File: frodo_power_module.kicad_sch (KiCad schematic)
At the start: 61 parts, among them J1 Keystone 1098, J10 SWD Header, J2 Molex MicroFit 2x2, J3 Molex MicroFit 2x2, J4 Molex MicroFit 2x2, J5 Molex MicroFit 2x2, J6 Molex MicroFit 2x2, J7 JST-GH, J8 JST-GH, J9 JST-GH, U1 STM32F042F6Px, U2 L7805, U3 AZ1117I-3.3, U4 BQ25171-Q1, U5 BQ29200, U6 MCP2562-E-SN, Y1 8MHz

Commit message: Add current sense amp to PCB
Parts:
- added C18, C19, C20: 100n, Capacitor_SMD:C_0603_1608Metric, symbol Device:C_Small
- added R18, R19: 10k, Resistor_SMD:R_0603_1608Metric, symbol Device:R_Small
- added R20, R22, R24: 1k8, Resistor_SMD:R_0603_1608Metric, symbol Device:R_Small
- added R21, R23: 1k, Resistor_SMD:R_0603_1608Metric, symbol Device:R_Small
- added U7: INA213, Package_TO_SOT_SMD:SOT-363_SC-70-6, symbol frodo_power_module:INA210
- R10, R14, R17: LCSC# C98220 -> (none); Part# RC0603FR-0710KL -> (none)
- R13: value TODO -> 5m
- R15: value 160 -> 120; LCSC# C98220 -> C114640; Part# RC0603FR-0710KL -> RC0603FR-07120RL
- R16: value 260 -> 220
- R2: LCSC# C114640 -> C98220; Part# RC0603FR-07120RL -> RC0603FR-0710KL
- R6: value 3.6k -> 1k8; LCSC# C98220 -> C185354; Part# RC0603FR-0710KL -> RC0603FR-071K8L
- R7, R8: value 1k -> 220
- R9: LCSC# C98220 -> (none); Manufacturer YAGEO -> (none); Part# RC0603FR-0710KL -> (none)
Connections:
- net +3V3: now also C18.2, C20.2, R18.2, U7.3 (V+)
- net +5V: now also C19.2
- net +BATT: now also U7.5 (-)
- net +VSW: now also R22.1
- net GND: now also C18.1, C19.1, C20.1, R19.1, R21.2, R23.2, R24.2, U7.2 (GND); no longer R6.2, R7.2
- net VDC: now also C12.1, D1.1 (K), JP1.1 (A), U4.1 (IN), R20.1; no longer D1.2 (A), J2.3 (Pin_3), J2.4 (Pin_4)
- net at R7.1, U4.2 (ISET): no longer R8.1
- net VSENSE_CHARGE: now reaches U1.12 (PA6)
- net VSENSE_CHARGE: now also R20.2, R21.1
- net VSENSE_BATT: now reaches U1.13 (PA7)
- net VSENSE_BATT: now also R22.2, R23.1
- net ISENSE: now reaches U1.14 (PB1)
- net ISENSE: now also U7.6
- net BATT_RAW: no longer names the net of J1.1 (Pin_1), R13.2, R14.2, R15.2
- net BATT_RAW: now also U7.4 (+)
- new net: R18.1, R19.2, U7.1 (REF)
- new net: R24.1, R6.2
- new net: R7.2, R8.1
- new net: D1.2 (A), J2.3 (Pin_3), J2.4 (Pin_4)
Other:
- note added: "ISET: 440 = 681mA"
- note added: "Icb1 = Vc1 / (Rcb + Rc1) Icb2 = (Vc2-Vc1) / (Rcb + Rvdd + Rc2) Icb1 = Icb2 => Rc1 = Rvdd + Rc2"
- note added: "max shunt drop: 3.3V (ADC range) / 2 (bidirectional) / 50 (INA gain) = 33mV max current: 33mV / 5mOhm = +/-6.6A, resolution: 6.6A/2048 = ~3.2mA"
- note removed: "ISET: 500 = 600mA"
- note removed: "TODO: Use current sense amplifier? INA210?"
- note removed: "TODO: pins for battery and charging voltage, current"
- moved on the sheet: C12, D1, R7, R8

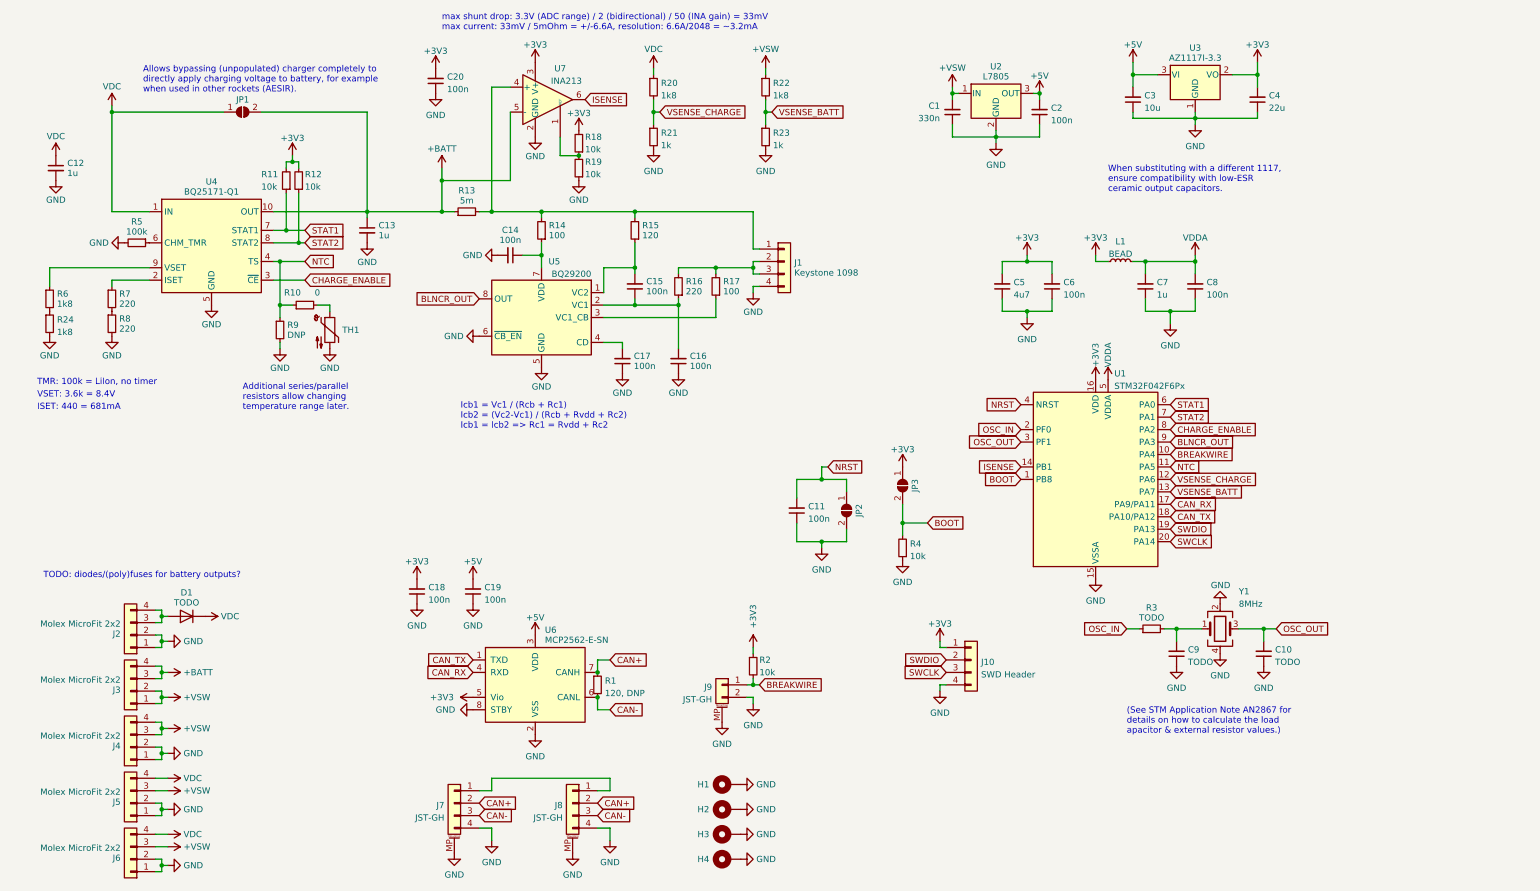
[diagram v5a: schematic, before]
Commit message: changed PCB
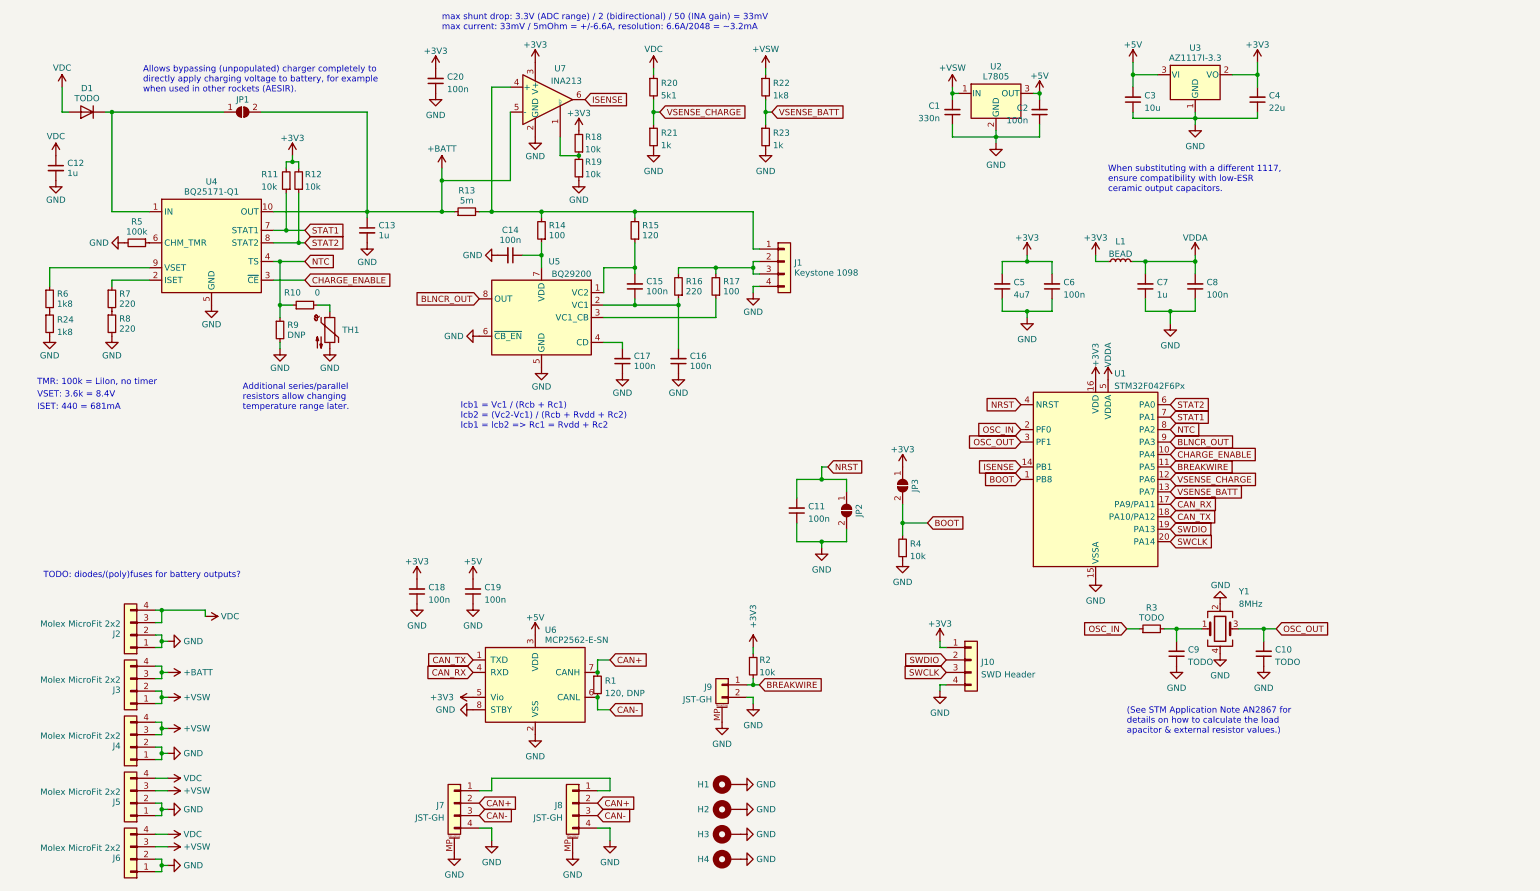
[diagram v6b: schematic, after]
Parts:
- R20: value 1k8 -> 5k1
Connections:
- net BREAKWIRE: now also U1.11 (PA5); no longer U1.10 (PA4)
- net CHARGE_ENABLE: now also U1.10 (PA4); no longer U1.8 (PA2)
- net NTC: now also U1.8 (PA2); no longer U1.11 (PA5)
- net STAT1: now also U1.7 (PA1); no longer U1.6 (PA0)
- net STAT2: now also U1.6 (PA0); no longer U1.7 (PA1)
- net VDC: now also D1.2 (A), J2.3 (Pin_3), J2.4 (Pin_4); no longer D1.1 (K), JP1.1 (A), U4.1 (IN)
- new net: D1.1 (K), JP1.1 (A), U4.1 (IN)
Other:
- moved on the sheet: C2, D1
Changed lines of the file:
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@@
   (junction (at 255.27 66.04) (diameter 0) (color 0 0 0 0)
   )
+  (junction (at 44.45 137.16) (diameter 0) (color 0 0 0 0)
+  )
   (junction (at 220.98 66.04) (diameter 0) (color 0 0 0 0)
   )
@@
   (junction (at 255.27 36.83) (diameter 0) (color 0 0 0 0)
   )
-  (junction (at 34.29 35.56) (diameter 0) (color 0 0 0 0)
-  )
   (junction (at 179.07 110.49) (diameter 0) (color 0 0 0 0)
   )
@@
   (junction (at 269.24 140.97) (diameter 0) (color 0 0 0 0)
   )
-  (junction (at 44.45 138.43) (diameter 0) (color 0 0 0 0)
-  )
   (junction (at 220.98 76.2) (diameter 0) (color 0 0 0 0)
   )
@@
   (junction (at 44.45 189.23) (diameter 0) (color 0 0 0 0)
   )
+  (junction (at 34.29 35.56) (diameter 0) (color 0 0 0 0)
+  )
   (junction (at 69.85 59.69) (diameter 0) (color 0 0 0 0)
   )
@@
     (stroke (width 0) (type default))
   )
-  (wire (pts (xy 44.45 137.16) (xy 44.45 138.43))
+  (wire (pts (xy 24.13 35.56) (xy 25.4 35.56))
+    (stroke (width 0) (type default))
+  )
+  (wire (pts (xy 44.45 137.16) (xy 44.45 139.7))
     (stroke (width 0) (type default))
   )
@@
     (stroke (width 0) (type default))
   )
-  (wire (pts (xy 45.72 138.43) (xy 44.45 138.43))
-    (stroke (width 0) (type default))
-  )
   (wire (pts (xy 44.45 160.02) (xy 43.18 160.02))
     (stroke (width 0) (type default))
@@
     (stroke (width 0) (type default))
   )
+  (wire (pts (xy 53.34 137.16) (xy 53.34 138.43))
+    (stroke (width 0) (type default))
+  )
   (wire (pts (xy 44.45 154.94) (xy 44.45 156.21))
     (stroke (width 0) (type default))
@@
     (stroke (width 0) (type default))
   )
-  (wire (pts (xy 44.45 138.43) (xy 44.45 139.7))
-    (stroke (width 0) (type default))
-  )
   (wire (pts (xy 220.98 76.2) (xy 220.98 77.47))
     (stroke (width 0) (type default))
@@
     (stroke (width 0) (type default))
   )
+  (wire (pts (xy 44.45 137.16) (xy 53.34 137.16))
+    (stroke (width 0) (type default))
+  )
   (wire (pts (xy 44.45 167.64) (xy 43.18 167.64))
     (stroke (width 0) (type default))
@@
     (stroke (width 0) (type default))
   )
-  (wire (pts (xy 34.29 34.29) (xy 34.29 35.56))
+  (wire (pts (xy 24.13 30.48) (xy 24.13 35.56))
     (stroke (width 0) (type default))
   )
@@
     (stroke (width 0) (type default))
   )
+  (wire (pts (xy 33.02 35.56) (xy 34.29 35.56))
+    (stroke (width 0) (type default))
+  )
   (wire (pts (xy 68.58 66.04) (xy 73.66 66.04))
     (stroke (width 0) (type default))
@@
     )
   )
-  (global_label "STAT2" (shape input) (at 250.19 97.79 0) (fields_autoplaced)
+  (global_label "STAT2" (shape input) (at 250.19 95.25 0) (fields_autoplaced)
     (effects (font (size 1.27 1.27)) (justify left))
-    (property "Intersheetrefs" "${INTERSHEET_REFS}" (at 258.5386 97.79 0)
+    (property "Intersheetrefs" "${INTERSHEET_REFS}" (at 258.5386 95.25 0)
       (effects (font (size 1.27 1.27)) (justify left) hide)
     )
@@
     )
   )
-  (global_label "STAT1" (shape input) (at 250.19 95.25 0) (fields_autoplaced)
+  (global_label "STAT1" (shape input) (at 250.19 97.79 0) (fields_autoplaced)
     (effects (font (size 1.27 1.27)) (justify left))
-    (property "Intersheetrefs" "${INTERSHEET_REFS}" (at 258.5386 95.25 0)
+    (property "Intersheetrefs" "${INTERSHEET_REFS}" (at 258.5386 97.79 0)
       (effects (font (size 1.27 1.27)) (justify left) hide)
     )
@@
     )
   )
-  (global_label "NTC" (shape input) (at 250.19 107.95 0) (fields_autoplaced)
+  (global_label "NTC" (shape input) (at 250.19 100.33 0) (fields_autoplaced)
     (effects (font (size 1.27 1.27)) (justify left))
-    (property "Intersheetrefs" "${INTERSHEET_REFS}" (at 256.6639 107.95 0)
+    (property "Intersheetrefs" "${INTERSHEET_REFS}" (at 256.6639 100.33 0)
       (effects (font (size 1.27 1.27)) (justify left) hide)
     )
@@
     )
   )
+  (global_label "BREAKWIRE" (shape input) (at 250.19 107.95 0) (fields_autoplaced)
+    (effects (font (size 1.27 1.27)) (justify left))
+    (property "Intersheetrefs" "${INTERSHEET_REFS}" (at 263.6186 107.95 0)
+      (effects (font (size 1.27 1.27)) (justify left) hide)
+    )
+  )
   (global_label "OSC_IN" (shape input) (at 219.71 100.33 180) (fields_autoplaced)
     (effects (font (size 1.27 1.27)) (justify right))
@@
     )
   )
-  (global_label "BREAKWIRE" (shape input) (at 250.19 105.41 0) (fields_autoplaced)
-    (effects (font (size 1.27 1.27)) (justify left))
-    (property "Intersheetrefs" "${INTERSHEET_REFS}" (at 263.6186 105.41 0)
-      (effects (font (size 1.27 1.27)) (justify left) hide)
-    )
-  )
   (global_label "OSC_OUT" (shape input) (at 219.71 102.87 180) (fields_autoplaced)
     (effects (font (size 1.27 1.27)) (justify right))
@@
     )
   )
+  (global_label "CHARGE_ENABLE" (shape input) (at 250.19 105.41 0) (fields_autoplaced)
+    (effects (font (size 1.27 1.27)) (justify left))
+    (property "Intersheetrefs" "${INTERSHEET_REFS}" (at 268.4567 105.41 0)
+      (effects (font (size 1.27 1.27)) (justify left) hide)
+    )
+  )
   (global_label "BLNCR_OUT" (shape input) (at 109.22 73.66 180) (fields_autoplaced)
     (effects (font (size 1.27 1.27)) (justify right))
@@
     )
   )
-  (global_label "CHARGE_ENABLE" (shape input) (at 250.19 100.33 0) (fields_autoplaced)
-    (effects (font (size 1.27 1.27)) (justify left))
-    (property "Intersheetrefs" "${INTERSHEET_REFS}" (at 268.4567 100.33 0)
-      (effects (font (size 1.27 1.27)) (justify left) hide)
-    )
-  )
   (global_label "BLNCR_OUT" (shape input) (at 250.19 102.87 0) (fields_autoplaced)
     (effects (font (size 1.27 1.27)) (justify left))
@@
     )
   )
-  (symbol (lib_id "Device:C_Small") (at 223.52 35.56 180) (unit 1)
-    (in_bom yes) (on_board yes) (dnp no) (fields_autoplaced)
-    (property "Reference" "C2" (at 225.8441 34.7189 0)
+  (symbol (lib_id "Device:C_Small") (at 223.52 35.56 0) (mirror x) (unit 1)
+    (in_bom yes) (on_board yes) (dnp no)
+    (property "Reference" "C2" (at 221.1959 34.7189 0)
       (effects (font (size 1.27 1.27)) (justify right))
     )
-    (property "Value" "100n" (at 225.8441 37.2558 0)
+    (property "Value" "100n" (at 221.1959 37.2558 0)
       (effects (font (size 1.27 1.27)) (justify right))
     )
@@
   )
   (symbol (lib_id "power:VDDA") (at 255.27 64.77 0) (unit 1)
-    (in_bom yes) (on_board yes) (dnp no) (fields_autoplaced)
+    (in_bom yes) (on_board yes) (dnp no)
     (property "Reference" "#PWR040" (at 255.27 68.58 0)
       (effects (font (size 1.27 1.27)) hide)
@@
     )
   )
-  (symbol (lib_id "Device:D") (at 49.53 138.43 180) (unit 1)
+  (symbol (lib_id "Device:D") (at 29.21 35.56 180) (unit 1)
     (in_bom yes) (on_board yes) (dnp no) (fields_autoplaced)
-    (property "Reference" "D1" (at 49.53 133.58 0)
+    (property "Reference" "D1" (at 29.21 30.71 0)
       (effects (font (size 1.27 1.27)))
     )
-    (property "Value" "TODO" (at 49.53 135.628 0)
+    (property "Value" "TODO" (at 29.21 32.758 0)
       (effects (font (size 1.27 1.27) (color 194 0 0 1)))
     )
-    (property "Footprint" "" (at 49.53 138.43 0)
+    (property "Footprint" "" (at 29.21 35.56 0)
       (effects (font (size 1.27 1.27)) hide)
     )
-    (property "Datasheet" "~" (at 49.53 138.43 0)
+    (property "Datasheet" "~" (at 29.21 35.56 0)
       (effects (font (size 1.27 1.27)) hide)
     )
-    (property "Sim.Device" "D" (at 49.53 138.43 0)
+    (property "Sim.Device" "D" (at 29.21 35.56 0)
       (effects (font (size 1.27 1.27)) hide)
     )
-    (property "Sim.Pins" "1=K 2=A" (at 49.53 138.43 0)
+    (property "Sim.Pins" "1=K 2=A" (at 29.21 35.56 0)
       (effects (font (size 1.27 1.27)) hide)
     )
@@
     )
   )
-  (symbol (lib_id "power:VDC") (at 34.29 34.29 0) (unit 1)
+  (symbol (lib_id "power:VDC") (at 24.13 30.48 0) (unit 1)
     (in_bom yes) (on_board yes) (dnp no) (fields_autoplaced)
-    (property "Reference" "#PWR011" (at 34.29 36.83 0)
+    (property "Reference" "#PWR011" (at 24.13 33.02 0)
       (effects (font (size 1.27 1.27)) hide)
     )
-    (property "Value" "VDC" (at 34.29 30.345 0)
+    (property "Value" "VDC" (at 24.13 26.535 0)
       (effects (font (size 1.27 1.27)))
     )
-    (property "Footprint" "" (at 34.29 34.29 0)
+    (property "Footprint" "" (at 24.13 30.48 0)
       (effects (font (size 1.27 1.27)) hide)
     )
-    (property "Datasheet" "" (at 34.29 34.29 0)
+    (property "Datasheet" "" (at 24.13 30.48 0)
       (effects (font (size 1.27 1.27)) hide)
     )
@@
       (effects (font (size 1.27 1.27)) (justify left))
     )
-    (property "Value" "1k8" (at 146.2786 32.1822 0)
+    (property "Value" "5k1" (at 146.2786 32.1822 0)
       (effects (font (size 1.27 1.27)) (justify left))
     )

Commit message: Update PCB design, add LEDs
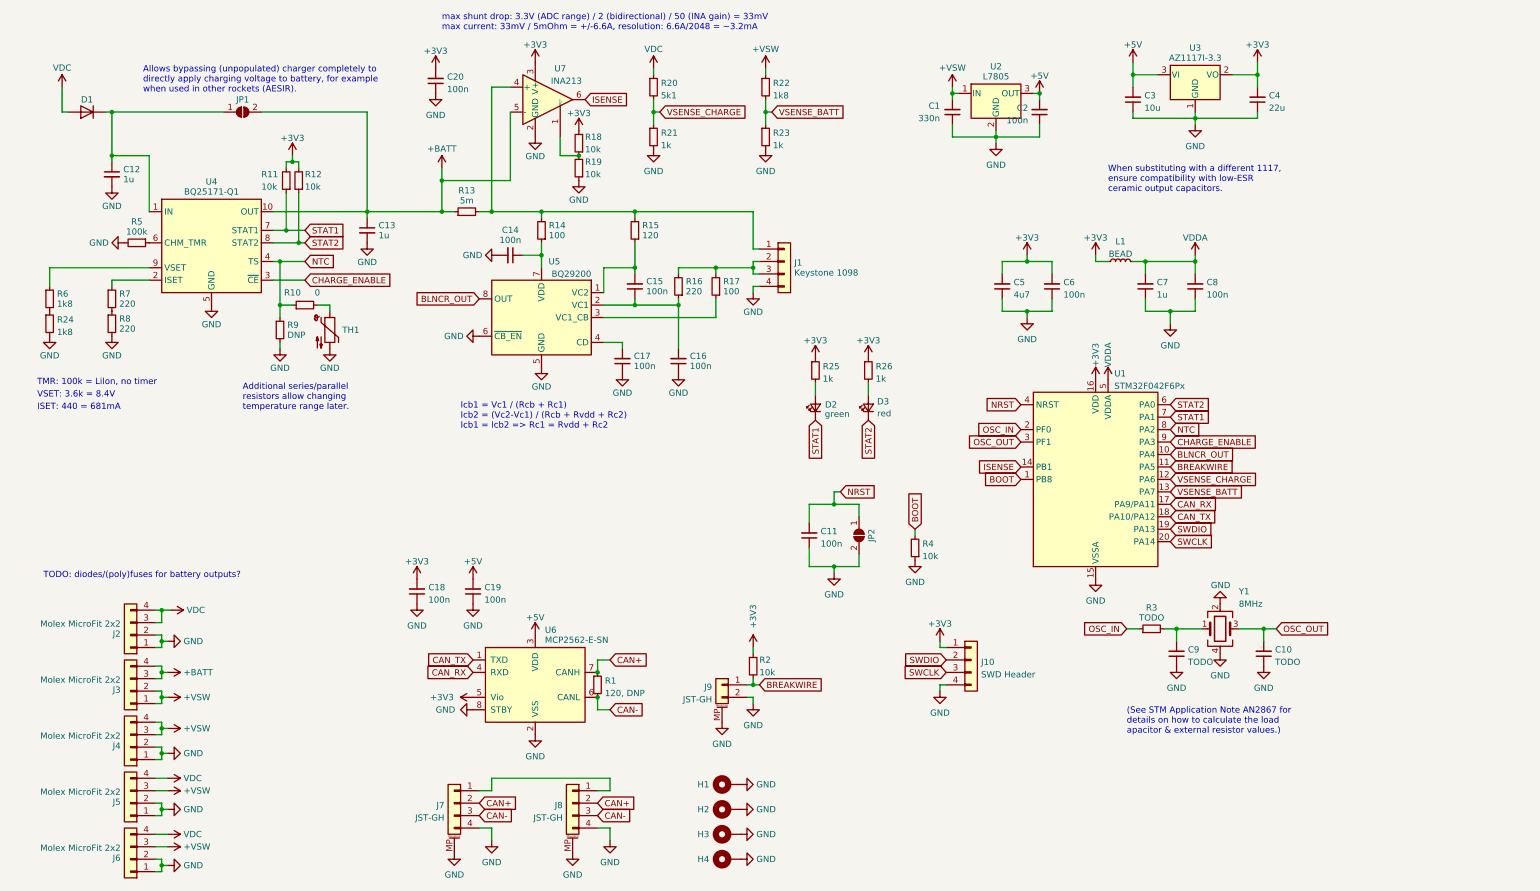
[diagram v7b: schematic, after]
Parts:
- removed JP3: SolderJumper_2_Open, Jumper:SolderJumper-2_P1.3mm_Open_RoundedPad1.0x1.5mm, symbol Jumper:SolderJumper_2_Open
- added D2: green, LED_SMD:LED_0603_1608Metric, symbol Device:LED_Small
- added D3: red, LED_SMD:LED_0603_1608Metric, symbol Device:LED_Small
- added R25, R26: 1k, Resistor_SMD:R_0603_1608Metric, symbol Device:R_Small
- D1: value TODO -> ~; footprint (none) -> Diode_SMD:D_SMA; DigiKey# (none) -> SK34A-LTPMSCT-ND
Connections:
- net +3V3: now also R25.1, R26.1
- net BLNCR_OUT: now also U1.10 (PA4); no longer U1.9 (PA3)
- net CHARGE_ENABLE: now also U1.9 (PA3); no longer U1.10 (PA4)
- net STAT1: now also D2.1 (K)
- net STAT2: now also D3.1 (K)
- net VDC: no longer C12.1
- net at D1.1 (K), JP1.1 (A), U4.1 (IN): now also C12.1
- new net: D3.2 (A), R26.2
- new net: D2.2 (A), R25.2
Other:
- moved on the sheet: C11, C12, JP2, R4
